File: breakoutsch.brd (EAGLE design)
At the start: 25 x 25 mm, 6 parts

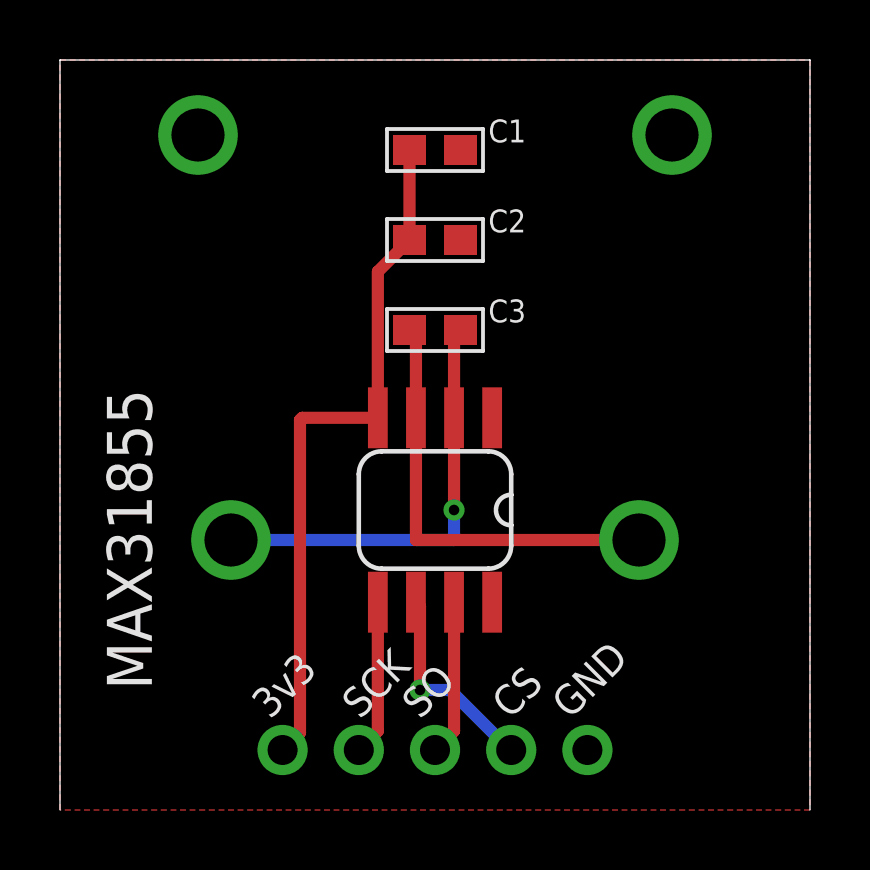
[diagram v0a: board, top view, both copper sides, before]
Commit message: update to pmod pinout as per http://www.digilentinc.com/Pmods/Digilent-Pmod_%20Interface_Specification.pdf
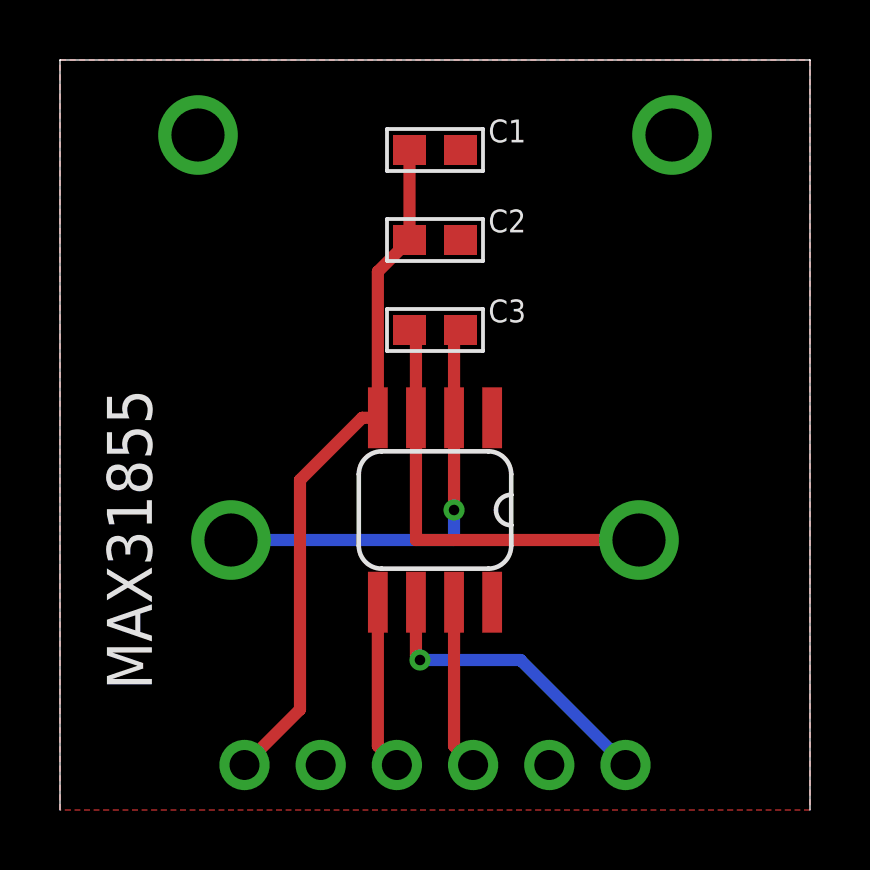
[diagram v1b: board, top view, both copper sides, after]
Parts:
- JP1: device nonolith:1X05_ROUND -> nonolith:1X06_ROUND
- moved JP1 0.50 mm to (12.5, 1.50), turned to 0 degrees
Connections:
- new net SI: JP1.5
- net 3V3: now also JP1.1; no longer JP1.5
- net CS: now also JP1.6; no longer JP1.2
- net GND: now also JP1.2; no longer JP1.1
- net SCK: now also JP1.3; no longer JP1.4
- net SO: now also JP1.4; no longer JP1.3
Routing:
- net CS: track 6.85 -> 10.3 mm
- net SO: track 5.19 -> 5.69 mm
- net SCK: track 5.19 -> 5.69 mm
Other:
- board text removed: "3v3"
- board text removed: "CS"
- board text removed: "GND"
- board text removed: "SCK"
- board text removed: "SO"
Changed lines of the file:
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@@
 <wire x1="25" y1="25" x2="0" y2="25" width="0" layer="20"/>
 <wire x1="0" y1="25" x2="0" y2="0" width="0" layer="20"/>
-<text x="7" y="3" size="1" layer="25" font="vector" ratio="12" rot="R45">3v3</text>
-<text x="10" y="3" size="1" layer="25" font="vector" ratio="12" rot="R45">SCK</text>
-<text x="12" y="3" size="1" layer="25" font="vector" ratio="12" rot="R45">SO</text>
-<text x="15" y="3" size="1" layer="25" font="vector" ratio="12" rot="R45">CS</text>
-<text x="17" y="3" size="1" layer="25" font="vector" ratio="12" rot="R45">GND</text>
 </plain>
 <attributes>
@@
 <attribute name="NAME" x="14.278" y="16.254" size="0.762" layer="25" font="vector" ratio="10"/>
 </element>
-<element name="JP1" library="nonolith" package="1X05_ROUND" value="" x="12.5" y="2" smashed="yes" rot="R180">
-<attribute name="VALUE" x="18.85" y="5.175" size="1.27" layer="27" rot="R180"/>
+<element name="JP1" library="nonolith" package="1X06_ROUND" value="" x="12.5" y="1.5" smashed="yes">
+<attribute name="VALUE" x="4.88" y="-1.675" size="1.27" layer="27"/>
 </element>
 </elements>
@@
 <contactref element="C2" pad="1"/>
 <contactref element="U$1" pad="4"/>
-<contactref element="JP1" pad="5"/>
 <wire x1="11.65" y1="19" x2="10.595" y2="17.945" width="0.4064" layer="1"/>
 <wire x1="10.595" y1="17.945" x2="10.595" y2="13.0734" width="0.4064" layer="1"/>
 <wire x1="11.65" y1="22" x2="11.65" y2="19" width="0.4064" layer="1"/>
-<wire x1="7.42" y1="2" x2="8" y2="2.58" width="0.4064" layer="1"/>
-<wire x1="8" y1="2.58" x2="8" y2="13" width="0.4064" layer="1"/>
-<wire x1="8" y1="13" x2="8.0734" y2="13.0734" width="0.4064" layer="1"/>
-<wire x1="8.0734" y1="13.0734" x2="10.595" y2="13.0734" width="0.4064" layer="1"/>
+<contactref element="JP1" pad="1"/>
+<wire x1="10.595" y1="13.0734" x2="10.0734" y2="13.0734" width="0.4064" layer="1"/>
+<wire x1="10.0734" y1="13.0734" x2="8" y2="11" width="0.4064" layer="1"/>
+<wire x1="8" y1="11" x2="8" y2="3.35" width="0.4064" layer="1"/>
+<wire x1="8" y1="3.35" x2="6.15" y2="1.5" width="0.4064" layer="1"/>
 </signal>
 <signal name="GND">
@@
 <contactref element="C2" pad="2"/>
 <contactref element="U$1" pad="1"/>
-<contactref element="JP1" pad="1"/>
 <polygon width="0.254" layer="1">
 <vertex x="0" y="25"/>
@@
 <contactref element="U$2" pad="GND@4"/>
 <contactref element="U$2" pad="GND@1"/>
+<contactref element="JP1" pad="2"/>
 </signal>
 <signal name="SCK">
 <contactref element="U$1" pad="5"/>
-<contactref element="JP1" pad="4"/>
-<wire x1="9.96" y1="2" x2="10.595" y2="2.635" width="0.4064" layer="1"/>
-<wire x1="10.595" y1="2.635" x2="10.595" y2="6.9266" width="0.4064" layer="1"/>
+<contactref element="JP1" pad="3"/>
+<wire x1="10.595" y1="2.135" x2="10.595" y2="6.9266" width="0.4064" layer="1"/>
+<wire x1="10.595" y1="2.135" x2="11.23" y2="1.5" width="0.4064" layer="1"/>
 </signal>
 <signal name="CS">
 <contactref element="U$1" pad="6"/>
-<contactref element="JP1" pad="2"/>
-<wire x1="11.865" y1="6.9266" x2="12" y2="6.7916" width="0.4064" layer="1"/>
-<wire x1="12" y1="6.7916" x2="12" y2="4" width="0.4064" layer="1"/>
-<via x="12" y="4" extent="1-16" drill="0.35" shape="octagon"/>
-<wire x1="12" y1="4" x2="13" y2="4" width="0.4064" layer="16"/>
-<wire x1="13" y1="4" x2="15" y2="2" width="0.4064" layer="16"/>
-<wire x1="15" y1="2" x2="15.04" y2="2" width="0.4064" layer="16"/>
+<contactref element="JP1" pad="6"/>
+<wire x1="11.865" y1="6.9266" x2="11.865" y2="5.135" width="0.4064" layer="1"/>
+<wire x1="11.865" y1="5.135" x2="12" y2="5" width="0.4064" layer="1"/>
+<via x="12" y="5" extent="1-16" drill="0.35" shape="octagon"/>
+<wire x1="12" y1="5" x2="15.35" y2="5" width="0.4064" layer="16"/>
+<wire x1="15.35" y1="5" x2="18.85" y2="1.5" width="0.4064" layer="16"/>
 </signal>
 <signal name="SO">
 <contactref element="U$1" pad="7"/>
-<contactref element="JP1" pad="3"/>
-<wire x1="12.5" y1="2" x2="13.135" y2="2.635" width="0.4064" layer="1"/>
-<wire x1="13.135" y1="2.635" x2="13.135" y2="6.9266" width="0.4064" layer="1"/>
+<contactref element="JP1" pad="4"/>
+<wire x1="13.135" y1="2.135" x2="13.135" y2="6.9266" width="0.4064" layer="1"/>
+<wire x1="13.135" y1="2.135" x2="13.77" y2="1.5" width="0.4064" layer="1"/>
+</signal>
+<signal name="SI">
+<contactref element="JP1" pad="5"/>
 </signal>
 </signals>
